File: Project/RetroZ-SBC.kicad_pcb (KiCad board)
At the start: 2 copper layers, 100 x 100 mm, 36 parts, among them J1 RetroZ-SBC_MasterBus, J2 PJ-102A, SW1 RESET, SW2 On/Off, U1 74HCT04, U10 Z84C3008PEG, U11 74LS138, U12 L7805CV-DG, U2 max699cpa, U3 74LS32, U4 74LS08, U5 Z80CPU, U6 74HC273, U7 74LS08-And2, U8 AT28C64B-15PU, U9 AS6C4008-55PCN, Y1 7.3728Mhz

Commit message: started the physical layout
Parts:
- moved C2 118.3 mm to (160.7, 44.5), turned to 90 degrees
- moved U2 116.6 mm to (74.9, 129.5)
- moved C1 115.9 mm to (144.1, 44.5), turned to 90 degrees
- moved J1 115.7 mm to (251.5, 97.8), turned to 270 degrees
- moved R2 113.6 mm to (160.0, 47.6), turned to 180 degrees
- moved R1 109.9 mm to (144.8, 47.6)
- moved U3 106.4 mm to (208.3, 63.5)
- moved U11 92.4 mm to (240.0, 121.9)
- moved U1 76.1 mm to (213.4, 120.7)
- moved U10 66.2 mm to (106.7, 100.3)
- moved U6 63.3 mm to (223.5, 55.9)
- moved Y1 62.4 mm to (152.4, 44.5)
- moved C6 58.6 mm to (251.5, 94.0)
- moved U4 52.1 mm to (213.4, 96.5)
- moved J2 44.9 mm to (77.5, 152.4)
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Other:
- copper layers 2 -> 4
- net class Default: clearance 0.2 -> 0.127; trace_width 0.25 -> 0.5; via_drill 0.4 -> 0.2
- rule trace_clearance: 0.2 -> 0.127
- rule trace_min: 0.2 -> 0.0889
- rule via_min_drill: 0.3 -> 0.2
- rule via_min_size: 0.4 -> 0.6

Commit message: started the layout
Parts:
- added REF**: 1pin, Connectors:1pin, F.Cu at (109.1, 144.9)
- added REF**: 1pin, Connectors:1pin, F.Cu at (109.1, 57.0)
- added REF**: 1pin, Connectors:1pin, F.Cu at (201.4, 57.0)
- added REF**: 1pin, Connectors:1pin, F.Cu at (201.4, 144.9)
- J1: value RetroZ-SBC_MasterBus -> Master Bus; footprint SystemBus:SystemBus_2x20_CCW -> SystemBus2:SHDR40W64P254_2X20_5130X500X865P
- J2: value PJ-102A -> POWER
- moved J1 145.5 mm to (110.0, 63.8), turned to 0 degrees
- moved U6 135.0 mm to (121.9, 144.8), turned to 90 degrees
- moved U11 125.1 mm to (120.0, 86.6)
- moved SW1 124.0 mm to (152.4, 141.6)
- moved J2 118.6 mm to (194.3, 132.1), turned to 270 degrees
- moved C7 104.6 mm to (117.5, 137.2), turned to 180 degrees
- moved SW2 95.2 mm to (186.1, 141.6)
- moved U2 90.4 mm to (165.1, 123.8)
- moved R4 87.8 mm to (120.0, 77.5)
- moved C10 83.9 mm to (197.5, 59.1), turned to 180 degrees
- moved C4 83.4 mm to (132.7, 99.1), turned to 270 degrees
- moved C3 81.3 mm to (120.0, 71.1), turned to 0 degrees
- moved C6 79.5 mm to (180.3, 58.4)
- moved R5 76.6 mm to (120.0, 80.0)
- moved R3 74.1 mm to (120.0, 74.9)
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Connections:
- net IOP0 renamed A0
- net IOP1 renamed A1
- net IOP2 renamed A2
- net IOP3 renamed A3
- net IO_SEL renamed A7
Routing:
- net /A13: track 0.00 -> 116.1 mm
- net RAM_A17: track 0.00 -> 88.4 mm, vias 0 -> 1
- net A7: track 0.00 -> 85.9 mm, vias 0 -> 2
- net A15: track 0.00 -> 84.6 mm, vias 0 -> 1
- net /A6: track 0.00 -> 84.5 mm, vias 0 -> 3
- net /A14: track 0.00 -> 84.3 mm, vias 0 -> 4
- net RAM_A16: track 0.00 -> 82.1 mm, vias 0 -> 2
- net /A11: track 0.00 -> 78.6 mm
- net /A5: track 0.00 -> 76.6 mm, vias 0 -> 4
- net RAM_A18: track 0.00 -> 73.8 mm, vias 0 -> 1
- net RAM_A15: track 0.00 -> 72.8 mm, vias 0 -> 1
- net /A10: track 0.00 -> 67.1 mm
- net /A8: track 0.00 -> 64.4 mm, vias 0 -> 1
- net /A9: track 0.00 -> 53.5 mm, vias 0 -> 1
- net /A12: track 0.00 -> 50.1 mm, vias 0 -> 1
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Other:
- board size 100 x 100 mm -> 99.7 x 95.2 mm
- board text added: "RetroZ-SBC rev. 1 J.P. Gravel, 2018 http://formix.org"

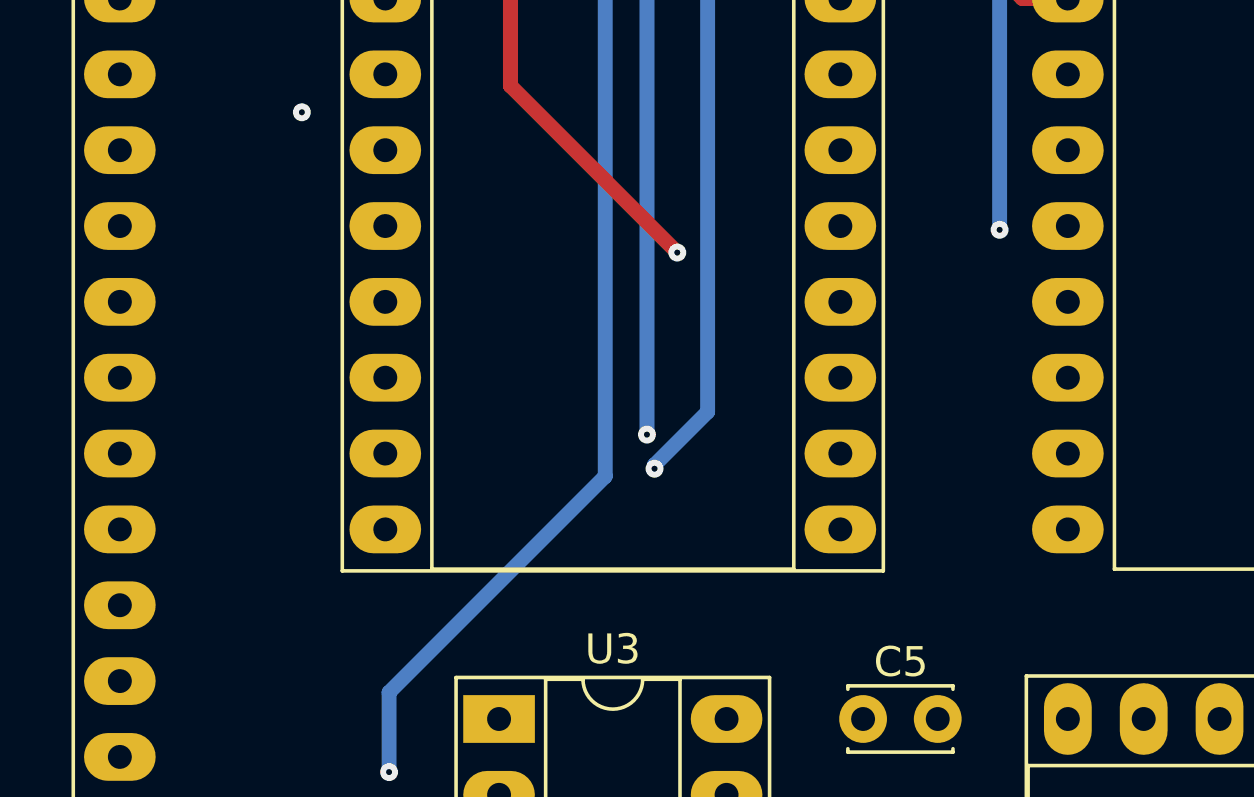
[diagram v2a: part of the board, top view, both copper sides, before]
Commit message: added some data wires
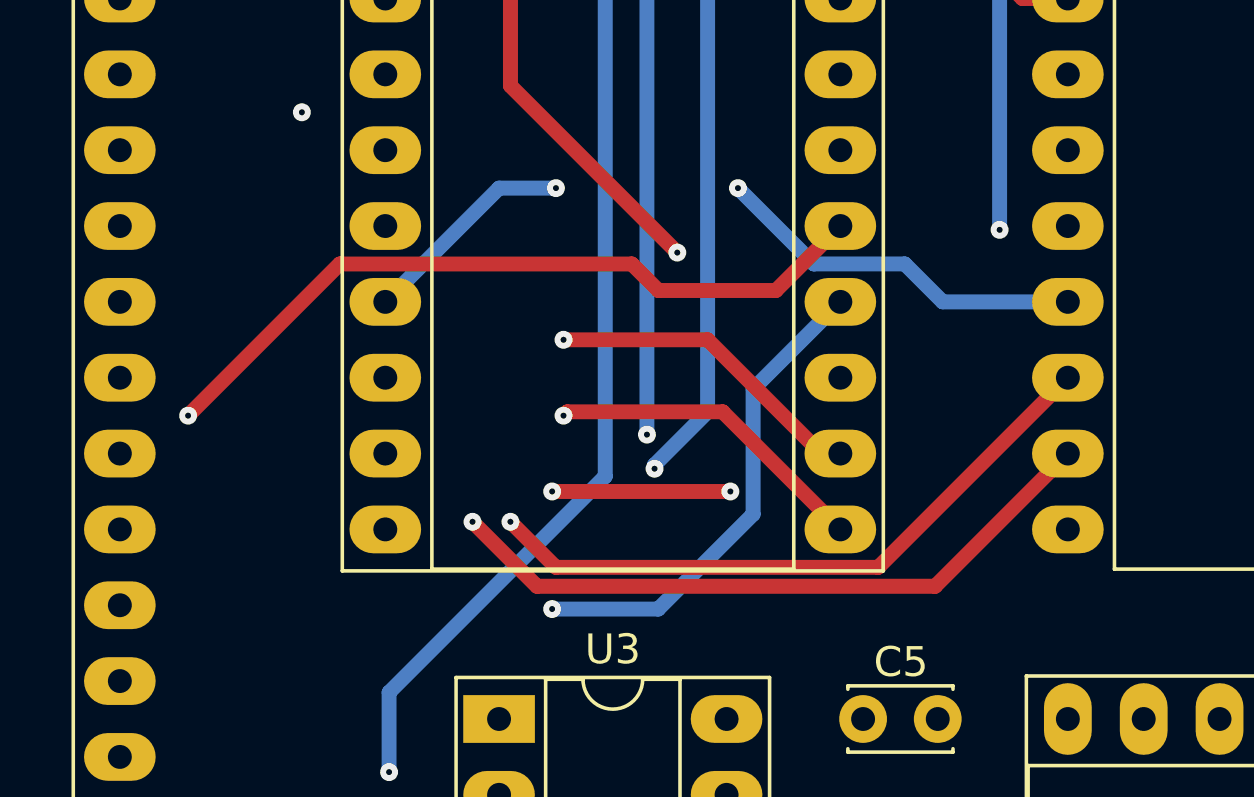
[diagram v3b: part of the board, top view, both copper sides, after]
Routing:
- net /D6: track 0.00 -> 78.2 mm, vias 0 -> 1
- net /D4: track 0.00 -> 76.9 mm, vias 0 -> 1
- net /D3: track 0.00 -> 76.2 mm, vias 0 -> 1
- net /D5: track 0.00 -> 72.6 mm, vias 0 -> 2
- net /D7: track 0.00 -> 68.2 mm, vias 0 -> 1
- net /D1: track 0.00 -> 55.8 mm, vias 0 -> 1
- net /D0: track 0.00 -> 51.2 mm, vias 0 -> 2
- net /D2: track 0.00 -> 26.5 mm, vias 0 -> 1

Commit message: fixed the ratnest!
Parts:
- moved C10 6.66 mm to (202.4, 63.5), turned to 270 degrees
- moved SW2 1.10 mm to (186.2, 142.7)
- moved C6 0.76 mm to (179.6, 58.4)
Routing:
- net Net-(R1-Pad1): track 2.54 -> 139.2 mm, vias 0 -> 2
- net Net-(C1-Pad1): track 16.5 -> 149.9 mm, vias 0 -> 3
- net /D3: track 76.2 -> 202.1 mm, vias 1 -> 4
- net /D2: track 26.5 -> 149.9 mm, vias 1 -> 4
- net /D4: track 76.9 -> 196.4 mm, vias 1 -> 4
- net /D5: track 72.6 -> 170.1 mm, vias 2 -> 3
- net RAM_A17: track 88.4 -> 0.00 mm, vias 1 -> 0
- net A15: track 84.6 -> 171.6 mm, vias 1 -> 2
- net /D6: track 78.2 -> 163.1 mm, vias 1 -> 3
- net RAM_A16: track 82.1 -> 0.13 mm, vias 2 -> 0
- net /D0: track 51.2 -> 127.4 mm, vias 2 -> 4
- net RAM_A18: track 73.8 -> 0.00 mm, vias 1 -> 0
- net RAM_A15: track 72.8 -> 0.00 mm, vias 1 -> 0
- net /D1: track 55.8 -> 126.8 mm, vias 1 -> 4
- net /D7: track 68.2 -> 136.6 mm, vias 1 -> 3
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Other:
- net class Default: trace_width 0.5 -> 0.2

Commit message: current state
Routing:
- net ~RESET: track 0.00 -> 197.8 mm, vias 0 -> 4
- net Net-(R1-Pad1): track 139.2 -> 272.0 mm, vias 2 -> 3
- net ~IO0: track 0.00 -> 119.0 mm, vias 0 -> 1
- net ~RD: track 0.00 -> 99.1 mm, vias 0 -> 2
- net RAMONLY: track 0.00 -> 92.6 mm, vias 0 -> 1
- net ~WR: track 0.00 -> 92.2 mm, vias 0 -> 4
- net RAM_A17: track 0.00 -> 84.0 mm, vias 0 -> 1
- net RAM_A15: track 0.00 -> 82.1 mm, vias 0 -> 3
- net RAM_A16: track 0.13 -> 80.9 mm, vias 0 -> 1
- net RAM_A18: track 0.00 -> 77.3 mm, vias 0 -> 1
- net Net-(U4-Pad3): track 0.00 -> 76.4 mm, vias 0 -> 1
- net Net-(U4-Pad6): track 0.00 -> 70.6 mm, vias 0 -> 3
- net ~MWR: track 0.00 -> 58.8 mm, vias 0 -> 2
- net Net-(U6-Pad2): track 0.00 -> 53.1 mm, vias 0 -> 2
- net ~MRD: track 0.00 -> 41.3 mm, vias 0 -> 1
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
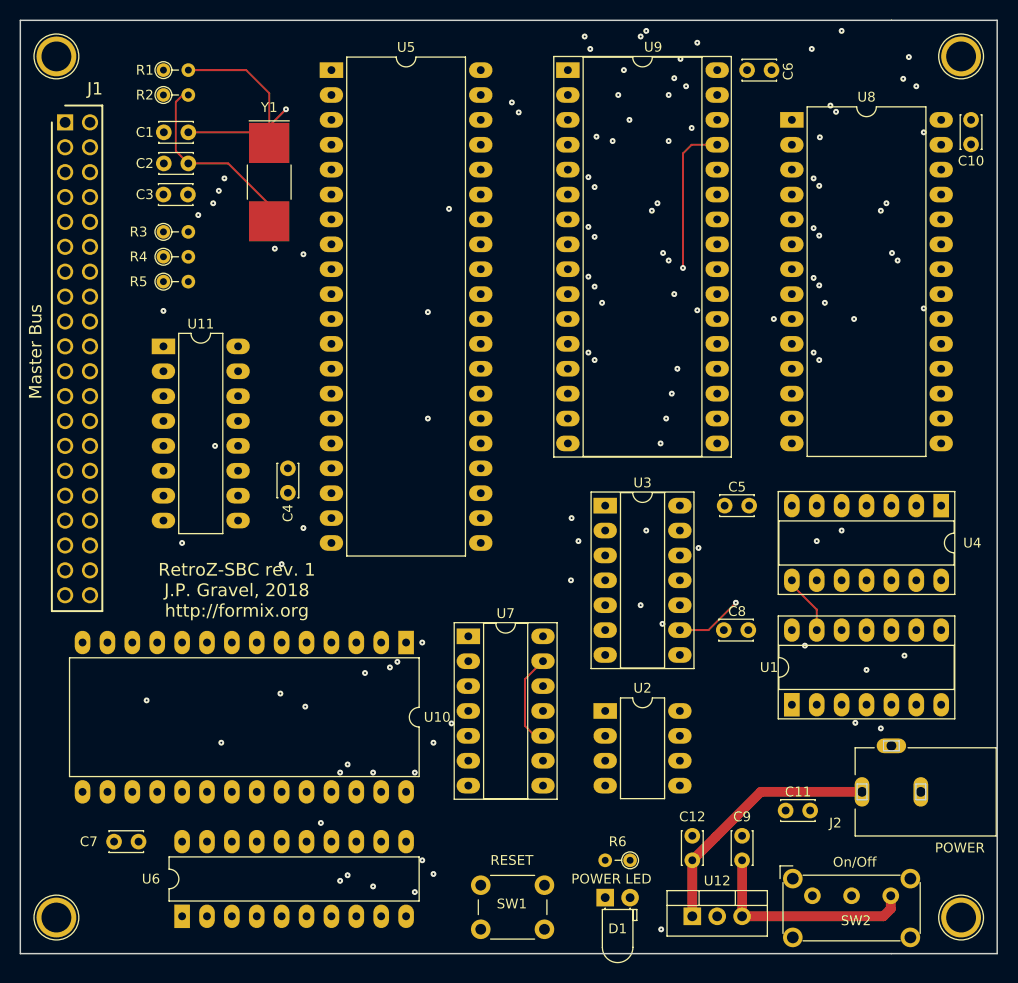
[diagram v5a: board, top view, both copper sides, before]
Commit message: new master bus design
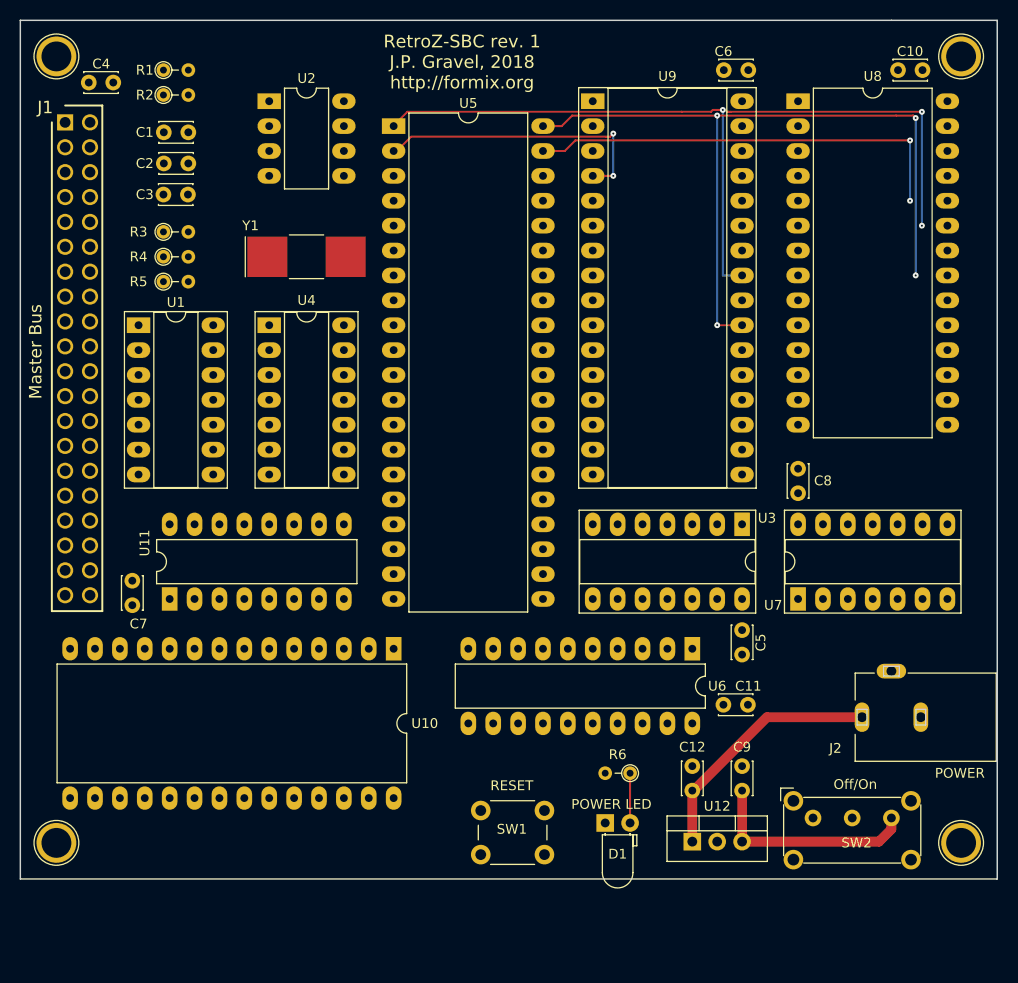
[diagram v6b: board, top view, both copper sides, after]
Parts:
- SW2: value On/Off -> Off/On
- moved U1 77.1 mm to (117.5, 84.5), turned to 0 degrees
- moved U2 71.1 mm to (130.8, 61.6)
- moved U4 71.0 mm to (130.8, 84.5), turned to 0 degrees
- moved U6 58.8 mm to (174.0, 117.5), turned to 270 degrees
- moved C4 44.3 mm to (112.4, 59.7), turned to 0 degrees
- moved U7 33.9 mm to (184.8, 112.4), turned to 90 degrees
- moved U11 25.8 mm to (120.7, 112.4), turned to 90 degrees
- moved C7 24.1 mm to (116.8, 113.0), turned to 90 degrees
- moved C8 14.9 mm to (184.8, 101.6), turned to 90 degrees
- moved U3 14.1 mm to (179.1, 104.8), turned to 270 degrees
- moved C5 12.8 mm to (179.1, 115.6), turned to 270 degrees
- moved C11 12.5 mm to (177.2, 123.2)
- moved R6 8.89 mm to (167.6, 130.2)
- moved U5 8.54 mm to (143.5, 64.1)
- moved Y1 8.52 mm to (134.6, 77.5), turned to 0 degrees
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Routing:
- net Net-(R1-Pad1): track 272.0 -> 0.00 mm, vias 3 -> 0
- net /D3: track 202.1 -> 0.00 mm, vias 5 -> 0
- net ~RESET: track 197.8 -> 0.00 mm, vias 4 -> 0
- net /D4: track 196.4 -> 0.00 mm, vias 5 -> 0
- net A15: track 191.2 -> 0.00 mm, vias 4 -> 0
- net /D2: track 149.9 -> 0.00 mm, vias 4 -> 0
- net Net-(C1-Pad1): track 149.9 -> 0.00 mm, vias 3 -> 0
- net /D5: track 145.7 -> 0.00 mm, vias 4 -> 0
- net /D6: track 139.2 -> 0.00 mm, vias 4 -> 0
- net /D7: track 136.6 -> 0.00 mm, vias 3 -> 0
- net /D0: track 127.4 -> 0.00 mm, vias 4 -> 0
- net /D1: track 126.8 -> 0.00 mm, vias 4 -> 0
- net A7: track 121.5 -> 0.00 mm, vias 4 -> 0
- net ~IO0: track 119.0 -> 0.00 mm, vias 1 -> 0
- net /A14: track 117.1 -> 0.00 mm, vias 3 -> 0
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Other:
- board size 99.7 x 95.2 mm -> 99.7 x 87.6 mm
